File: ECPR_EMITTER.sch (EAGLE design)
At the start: 17 parts, among them IC1 78L05, IC2 ATMEGA8-PU, J1 0802_SCREEN, Q1 BFR96, U1 AD9850 DDS Module

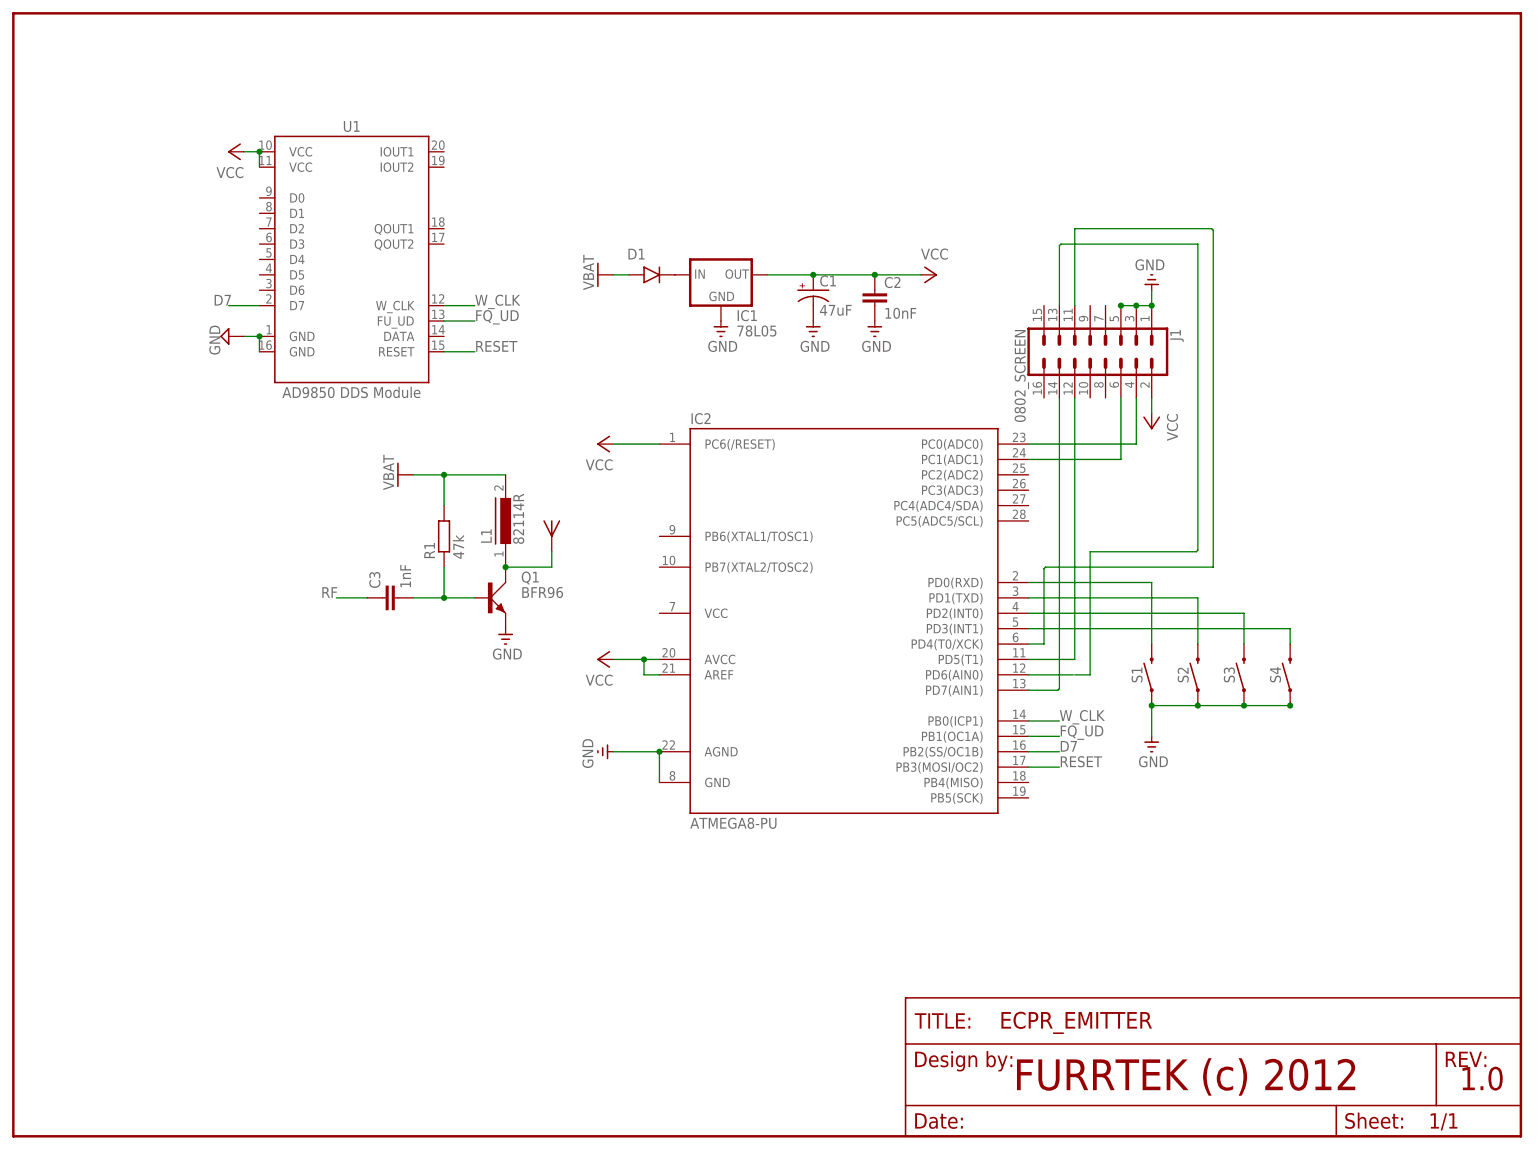
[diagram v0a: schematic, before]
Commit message: feat(board): final version w/ led, switch, pads for battery, rf connected, new version of AD9850 libs
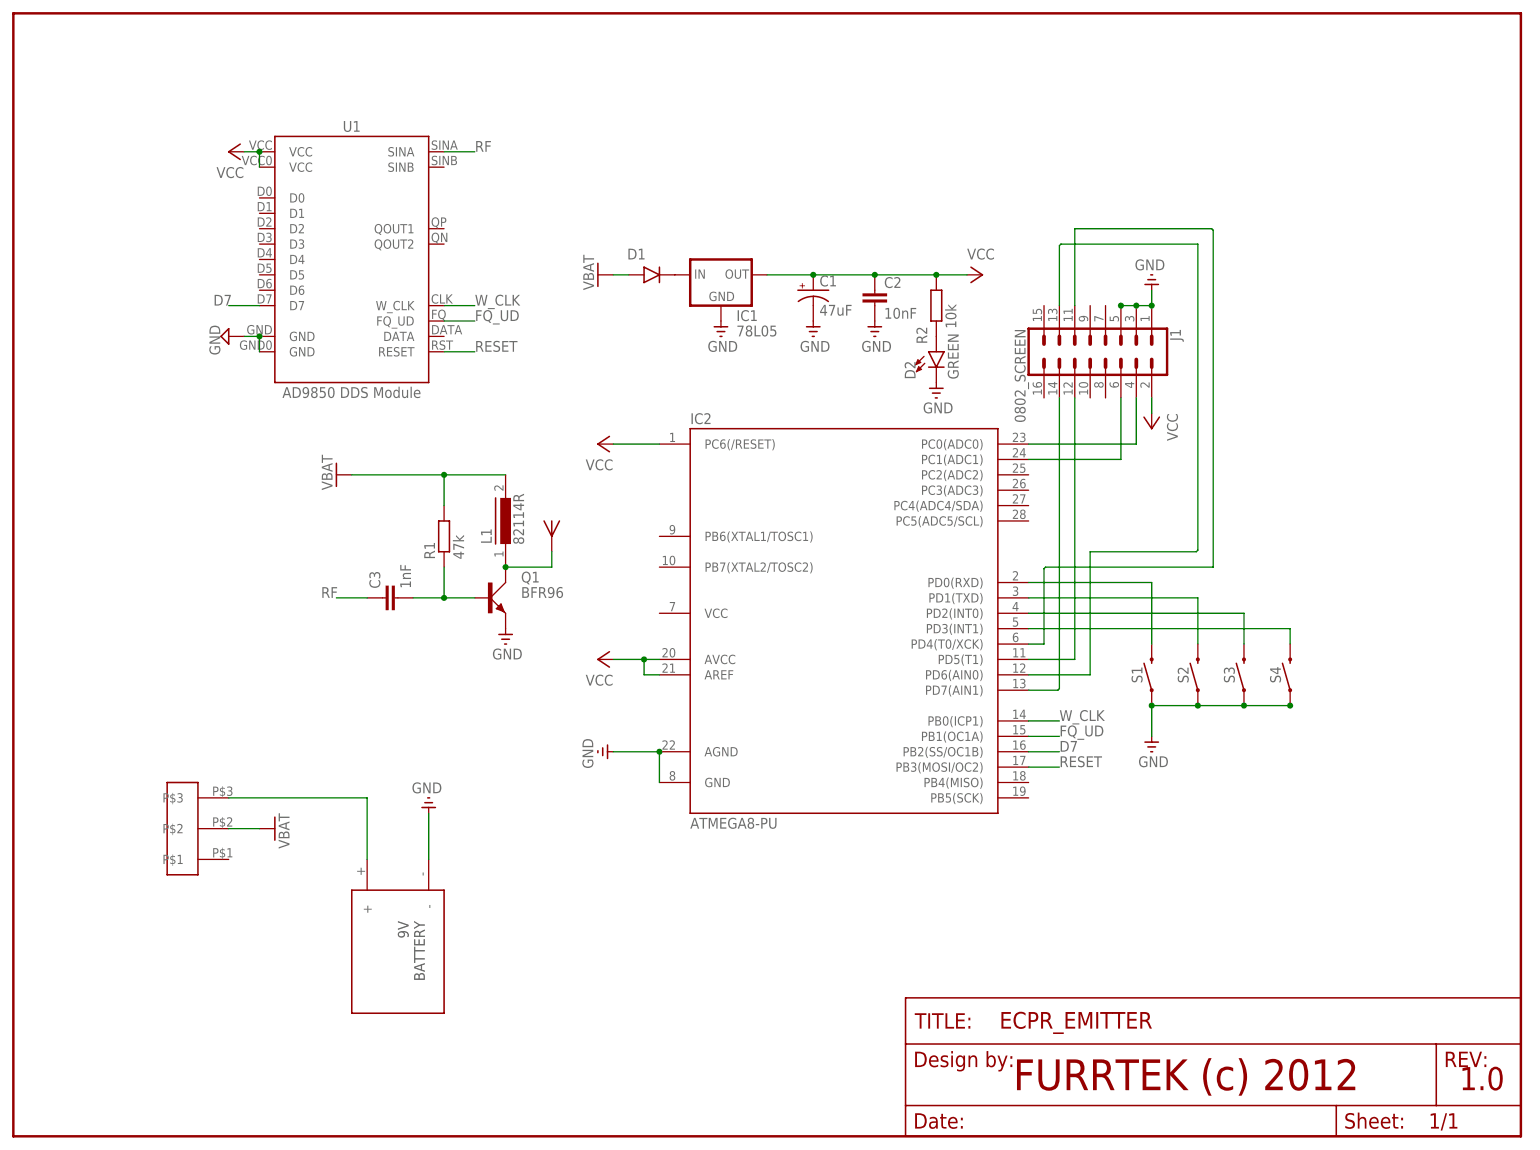
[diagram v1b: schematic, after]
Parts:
- added D2: GREEN, SparkFun-LED:LED-3MM-NO_SILK
- added R2: 10k, resistor:R-EU_0207/7
- added U$2: PACKAGESWITCH, SLIDESWITCH:PACKAGESWITCH
- added U$3: BAT, BATTERY:BAT
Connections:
- new net N$16: D2.A, R2.1
- net FQ_UD: now also U1.FQ_UD; no longer U1.FU_UD
- net GND: now also D2.C, U$3.-, U1.GND@P11, U1.GND@P6; no longer U1.GND@P1, U1.GND@P16
- net N$12: now also U$2.P$3, U$3.+; no longer IC2.PD6(AIN0)
- net N$13: now also IC2.PD6(AIN0)
- net RF: now also U1.SINA
- net VBAT: now also U$2.P$2
- net VCC: now also R2.2, U1.VCC@P1, U1.VCC@P20; no longer U1.VCC@P10, U1.VCC@P11
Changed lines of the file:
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@@
 <part name="FRAME1" library="SparkFun-Aesthetics" deviceset="FRAME-LETTER" device="NO_PACKAGE"/>
 <part name="GND7" library="supply0" deviceset="GND" device=""/>
+<part name="D2" library="SparkFun-LED" deviceset="LED" device="-3MM-NO_SILK" value="GREEN"/>
+<part name="R2" library="resistor" deviceset="R-EU_" device="0207/7" value="10k"/>
+<part name="U$2" library="SLIDESWITCH" deviceset="PACKAGESWITCH" device=""/>
+<part name="U$3" library="BATTERY" deviceset="BAT" device=""/>
+<part name="GND8" library="supply" deviceset="GND" device=""/>
+<part name="GND9" library="supply0" deviceset="GND" device=""/>
+<part name="V3" library="supply0" deviceset="VBAT" device=""/>
 </parts>
 <sheets>
@@
 <attribute name="VALUE" x="143.764" y="135.001" size="1.778" layer="96" font="vector"/>
 </instance>
-<instance part="P+1" gate="VCC" x="152.4" y="142.24" smashed="yes" rot="R270">
-<attribute name="VALUE" x="149.86" y="144.78" size="1.778" layer="96"/>
+<instance part="P+1" gate="VCC" x="160.02" y="142.24" smashed="yes" rot="R270">
+<attribute name="VALUE" x="157.48" y="144.78" size="1.778" layer="96"/>
 </instance>
 <instance part="P+2" gate="VCC" x="187.96" y="116.84" smashed="yes" rot="R180">
@@
 <attribute name="VALUE" x="65.659" y="90.424" size="1.778" layer="96" rot="R90"/>
 </instance>
-<instance part="V1" gate="G$1" x="63.5" y="109.22" smashed="yes" rot="R90">
-<attribute name="VALUE" x="62.865" y="106.68" size="1.778" layer="96" ratio="12" rot="R90"/>
+<instance part="V1" gate="G$1" x="53.34" y="109.22" smashed="yes" rot="R90">
+<attribute name="VALUE" x="52.705" y="106.68" size="1.778" layer="96" ratio="12" rot="R90"/>
 </instance>
 <instance part="V2" gate="G$1" x="96.52" y="142.24" smashed="yes" rot="R90">
@@
 <instance part="GND7" gate="1" x="96.52" y="63.5" smashed="yes" rot="R270">
 <attribute name="VALUE" x="93.98" y="65.7225" size="1.778" layer="96" ratio="12" rot="R270"/>
+</instance>
+<instance part="D2" gate="G$1" x="152.4" y="129.54" smashed="yes">
+<attribute name="NAME" x="148.971" y="124.968" size="1.778" layer="95" font="vector" rot="R90"/>
+<attribute name="VALUE" x="154.305" y="124.968" size="1.778" layer="96" font="vector" rot="R90" align="top-left"/>
+</instance>
+<instance part="R2" gate="G$1" x="152.4" y="137.16" smashed="yes" rot="R90">
+<attribute name="NAME" x="150.9014" y="130.81" size="1.778" layer="95" rot="R90"/>
+<attribute name="VALUE" x="155.702" y="133.35" size="1.778" layer="96" rot="R90"/>
+</instance>
+<instance part="U$2" gate="G$1" x="30.48" y="48.26" smashed="yes" rot="R180"/>
+<instance part="U$3" gate="BATTERY" x="55.88" y="43.18" smashed="yes" rot="R270"/>
+<instance part="GND8" gate="1" x="152.4" y="121.92" smashed="yes">
+<attribute name="VALUE" x="150.1775" y="119.38" size="1.778" layer="96"/>
+</instance>
+<instance part="GND9" gate="1" x="68.58" y="55.88" smashed="yes" rot="R180">
+<attribute name="VALUE" x="70.8025" y="58.42" size="1.778" layer="96" ratio="12" rot="R180"/>
+</instance>
+<instance part="V3" gate="G$1" x="43.18" y="50.8" smashed="yes" rot="R270">
+<attribute name="VALUE" x="43.815" y="53.34" size="1.778" layer="96" ratio="12" rot="R270"/>
 </instance>
 </instances>
@@
 </segment>
 <segment>
-<pinref part="U1" gate="G$1" pin="GND@P16"/>
-<pinref part="U1" gate="G$1" pin="GND@P1"/>
+<pinref part="U1" gate="G$1" pin="GND@P6"/>
+<pinref part="U1" gate="G$1" pin="GND@P11"/>
 <wire x1="40.64" y1="129.54" x2="40.64" y2="132.08" width="0.1524" layer="91"/>
 <pinref part="SUPPLY1" gate="GND" pin="GND"/>
@@
 <junction x="106.68" y="63.5"/>
 </segment>
+<segment>
+<pinref part="GND8" gate="1" pin="GND"/>
+<pinref part="D2" gate="G$1" pin="C"/>
+</segment>
+<segment>
+<pinref part="U$3" gate="BATTERY" pin="-"/>
+<wire x1="68.58" y1="45.72" x2="68.58" y2="53.34" width="0.1524" layer="91"/>
+<pinref part="GND9" gate="1" pin="GND"/>
+</segment>
 </net>
 <net name="N$1" class="0">
@@
 <junction x="132.08" y="142.24"/>
 <pinref part="P+1" gate="VCC" pin="VCC"/>
-<wire x1="142.24" y1="142.24" x2="149.86" y2="142.24" width="0.1524" layer="91"/>
+<wire x1="142.24" y1="142.24" x2="152.4" y2="142.24" width="0.1524" layer="91"/>
 <junction x="142.24" y="142.24"/>
+<pinref part="R2" gate="G$1" pin="2"/>
+<wire x1="152.4" y1="142.24" x2="157.48" y2="142.24" width="0.1524" layer="91"/>
+<junction x="152.4" y="142.24"/>
 </segment>
 <segment>
@@
 <segment>
 <pinref part="P+5" gate="VCC" pin="VCC"/>
-<pinref part="U1" gate="G$1" pin="VCC@P10"/>
+<pinref part="U1" gate="G$1" pin="VCC@P20"/>
 <wire x1="38.1" y1="162.56" x2="40.64" y2="162.56" width="0.1524" layer="91"/>
-<pinref part="U1" gate="G$1" pin="VCC@P11"/>
+<pinref part="U1" gate="G$1" pin="VCC@P1"/>
 <wire x1="40.64" y1="160.02" x2="40.64" y2="162.56" width="0.1524" layer="91"/>
 <junction x="40.64" y="162.56"/>
@@
 <wire x1="71.12" y1="109.22" x2="71.12" y2="104.14" width="0.1524" layer="91"/>
 <pinref part="V1" gate="G$1" pin="VBAT"/>
-<wire x1="66.04" y1="109.22" x2="71.12" y2="109.22" width="0.1524" layer="91"/>
+<wire x1="55.88" y1="109.22" x2="71.12" y2="109.22" width="0.1524" layer="91"/>
 <junction x="71.12" y="109.22"/>
+</segment>
+<segment>
+<pinref part="U$2" gate="G$1" pin="P$2"/>
+<wire x1="35.56" y1="50.8" x2="40.64" y2="50.8" width="0.1524" layer="91"/>
+<pinref part="V3" gate="G$1" pin="VBAT"/>
 </segment>
 </net>
@@
 <wire x1="172.974" y1="147.32" x2="172.72" y2="147.066" width="0.1524" layer="91"/>
 <wire x1="195.58" y1="147.32" x2="172.974" y2="147.32" width="0.1524" layer="91"/>
-<wire x1="175.26" y1="76.2" x2="177.8" y2="76.2" width="0.1524" layer="91"/>
 <wire x1="177.8" y1="76.2" x2="177.8" y2="96.52" width="0.1524" layer="91"/>
+<pinref part="IC2" gate="1" pin="PD6(AIN0)"/>
+<wire x1="167.64" y1="76.2" x2="177.8" y2="76.2" width="0.1524" layer="91"/>
 </segment>
 </net>
@@
 <label x="50.8" y="88.9" size="1.778" layer="95"/>
 </segment>
+<segment>
+<pinref part="U1" gate="G$1" pin="SINA"/>
+<wire x1="71.12" y1="162.56" x2="76.2" y2="162.56" width="0.1524" layer="91"/>
+<label x="76.2" y="162.56" size="1.778" layer="95"/>
+</segment>
 </net>
 <net name="FQ_UD" class="0">
 <segment>
-<pinref part="U1" gate="G$1" pin="FU_UD"/>
+<pinref part="U1" gate="G$1" pin="FQ_UD"/>
 <wire x1="71.12" y1="134.62" x2="76.2" y2="134.62" width="0.1524" layer="91"/>
 <label x="76.2" y="134.62" size="1.778" layer="95"/>
@@
 </segment>
 </net>
+<net name="N$16" class="0">
+<segment>
+<pinref part="R2" gate="G$1" pin="1"/>
+<pinref part="D2" gate="G$1" pin="A"/>
+</segment>
+</net>
 <net name="N$12" class="0">
 <segment>
-<pinref part="IC2" gate="1" pin="PD6(AIN0)"/>
-<wire x1="167.64" y1="76.2" x2="175.006" y2="76.2" width="0.1524" layer="91"/>
-</segment>
-</net>
+<pinref part="U$2" gate="G$1" pin="P$3"/>
+<pinref part="U$3" gate="BATTERY" pin="+"/>
+<wire x1="35.56" y1="55.88" x2="58.42" y2="55.88" width="0.1524" layer="91"/>
+<wire x1="58.42" y1="55.88" x2="58.42" y2="45.72" width="0.1524" layer="91"/>
+</segment>
+</net>

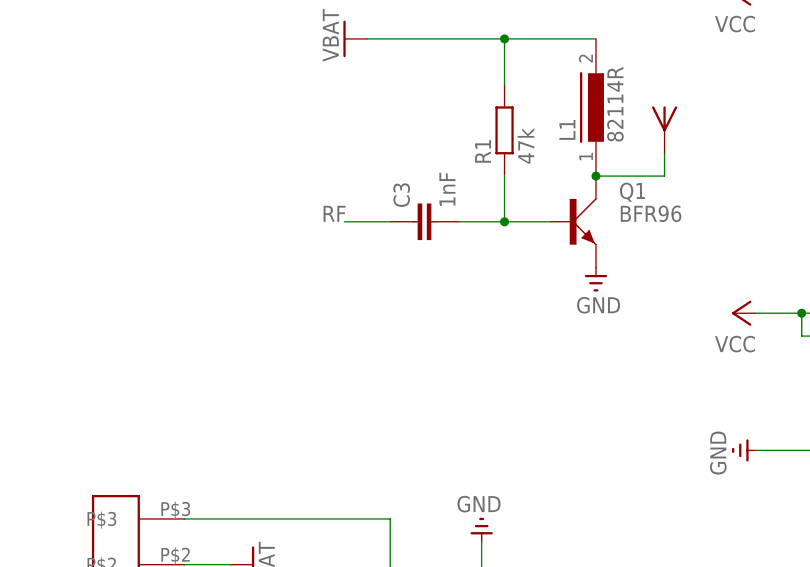
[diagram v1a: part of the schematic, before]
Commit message: feat(testpin): add rf out and update to eagle 9.4.0
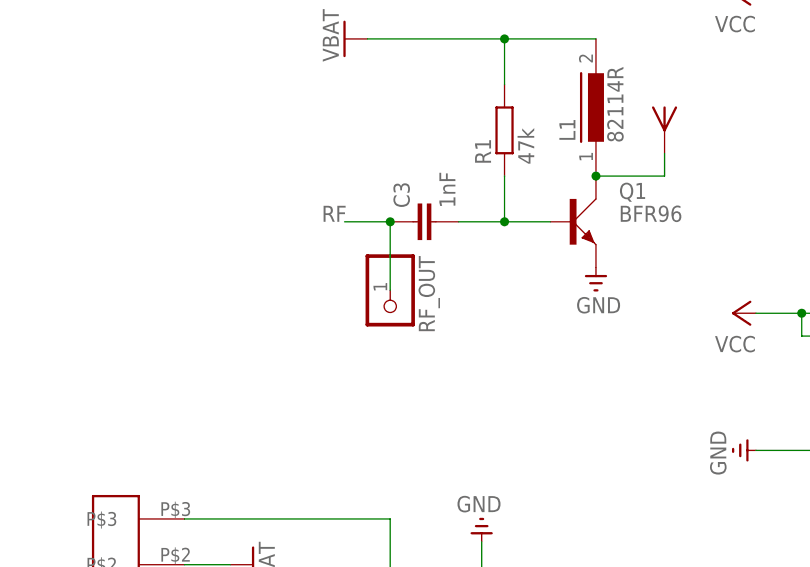
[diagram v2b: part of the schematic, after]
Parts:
- added RF_OUT: (no value), adafruit:PINHD-1X1
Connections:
- net RF: now also RF_OUT.1
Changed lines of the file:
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@@
 <?xml version="1.0" encoding="utf-8"?>
 <!DOCTYPE eagle SYSTEM "eagle.dtd">
-<eagle version="9.3.2">
+<eagle version="9.4.0">
 <drawing>
 <settings>
@@
 <part name="GND9" library="supply0" deviceset="GND" device=""/>
 <part name="V3" library="supply0" deviceset="VBAT" device=""/>
+<part name="RF_OUT" library="adafruit" deviceset="PINHD-1X1" device=""/>
 </parts>
 <sheets>
@@
 <instance part="V3" gate="G$1" x="43.18" y="50.8" smashed="yes" rot="R270">
 <attribute name="VALUE" x="43.815" y="53.34" size="1.778" layer="96" ratio="12" rot="R270"/>
+</instance>
+<instance part="RF_OUT" gate="G$1" x="58.42" y="78.74" smashed="yes" rot="R270">
+<attribute name="NAME" x="61.595" y="85.09" size="1.778" layer="95" rot="R270"/>
+<attribute name="VALUE" x="53.34" y="85.09" size="1.778" layer="96" rot="R270"/>
 </instance>
 </instances>
@@
 <wire x1="58.42" y1="88.9" x2="53.34" y2="88.9" width="0.1524" layer="91"/>
 <label x="50.8" y="88.9" size="1.778" layer="95"/>
-</segment>
-<segment>
+<pinref part="RF_OUT" gate="G$1" pin="1"/>
+<wire x1="58.42" y1="81.28" x2="58.42" y2="88.9" width="0.1524" layer="91"/>
+<junction x="58.42" y="88.9"/>
+</segment>
+<segment>

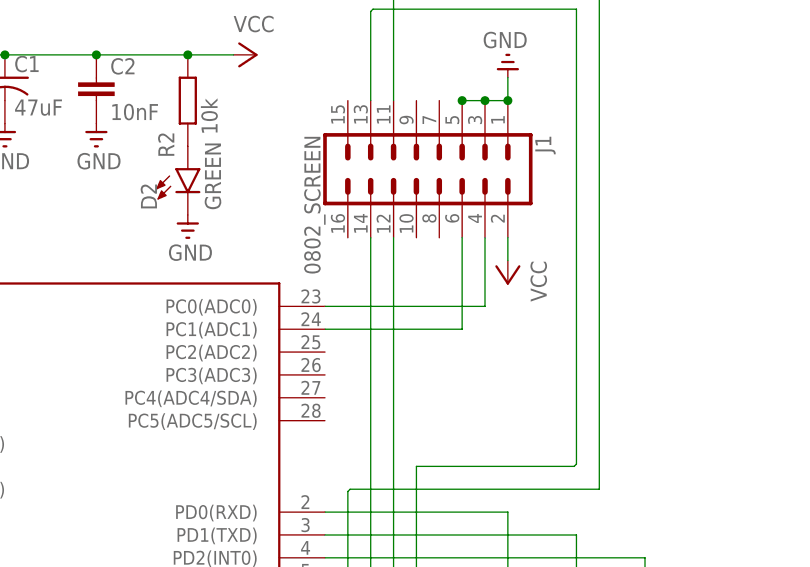
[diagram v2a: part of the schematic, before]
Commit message: fix: screen orientation & pin23/24
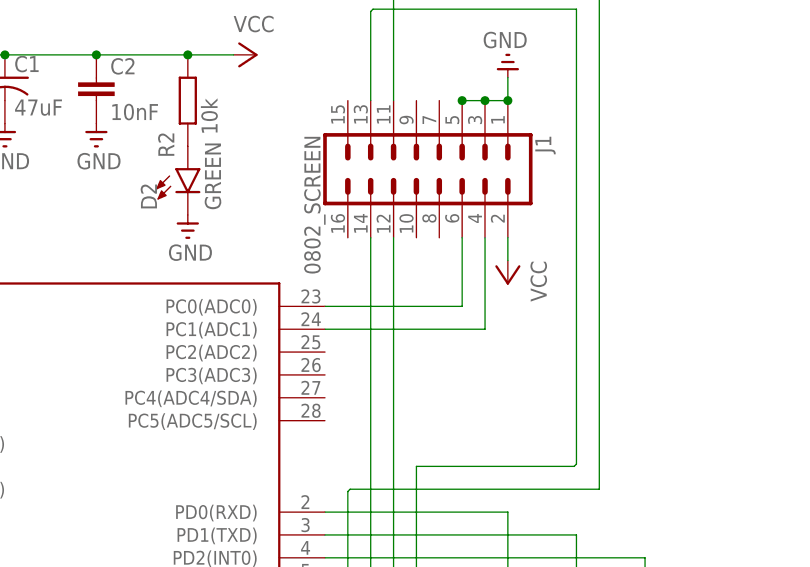
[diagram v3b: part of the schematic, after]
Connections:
- net N$8: now also IC2.PC1(ADC1); no longer IC2.PC0(ADC0)
- net N$9: now also IC2.PC0(ADC0); no longer IC2.PC1(ADC1)
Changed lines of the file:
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@@
 <?xml version="1.0" encoding="utf-8"?>
 <!DOCTYPE eagle SYSTEM "eagle.dtd">
-<eagle version="9.4.0">
+<eagle version="9.4.2">
 <drawing>
 <settings>
@@
 <segment>
 <pinref part="J1" gate="G$1" pin="4"/>
-<pinref part="IC2" gate="1" pin="PC0(ADC0)"/>
-<wire x1="185.42" y1="121.92" x2="185.42" y2="114.3" width="0.1524" layer="91"/>
-<wire x1="185.42" y1="114.3" x2="167.64" y2="114.3" width="0.1524" layer="91"/>
-</segment>
-</net>
-<net name="N$9" class="0">
-<segment>
-<pinref part="J1" gate="G$1" pin="6"/>
+<wire x1="185.42" y1="121.92" x2="185.42" y2="111.76" width="0.1524" layer="91"/>
 <pinref part="IC2" gate="1" pin="PC1(ADC1)"/>
-<wire x1="182.88" y1="121.92" x2="182.88" y2="111.76" width="0.1524" layer="91"/>
-<wire x1="182.88" y1="111.76" x2="167.64" y2="111.76" width="0.1524" layer="91"/>
+<wire x1="185.42" y1="111.76" x2="167.64" y2="111.76" width="0.1524" layer="91"/>
 </segment>
 </net>
@@
 </segment>
 </net>
+<net name="N$9" class="0">
+<segment>
+<pinref part="J1" gate="G$1" pin="6"/>
+<pinref part="IC2" gate="1" pin="PC0(ADC0)"/>
+<wire x1="182.88" y1="121.92" x2="182.88" y2="114.3" width="0.1524" layer="91"/>
+<wire x1="182.88" y1="114.3" x2="167.64" y2="114.3" width="0.1524" layer="91"/>
+</segment>
+</net>
